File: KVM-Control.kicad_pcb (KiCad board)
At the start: 2 copper layers, 14 parts, among them J1 KVM 1, J2 KVM 2, J3 KVM 2, U1 ESP32-S3-DevKitC, U2 ULN2003A, U3 PC847, U5 L7805

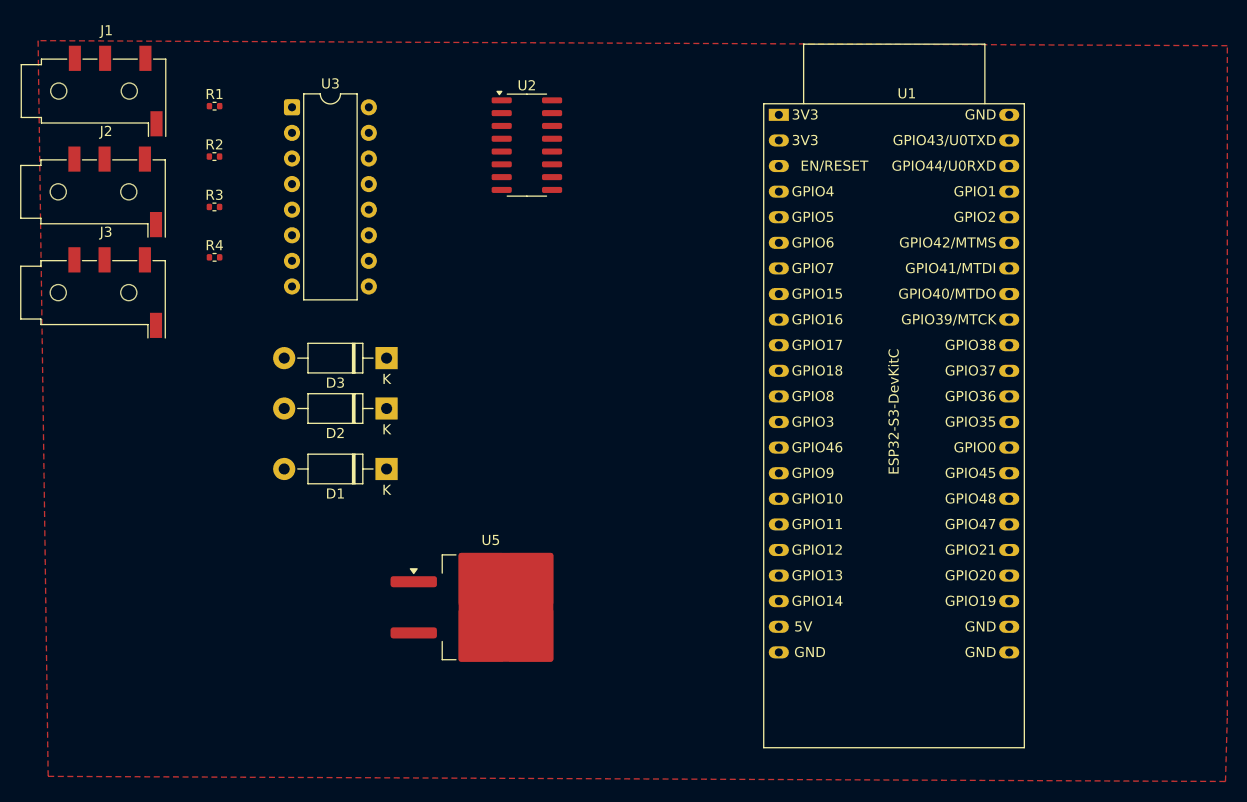
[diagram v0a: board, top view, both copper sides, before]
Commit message: Added status LEDs.
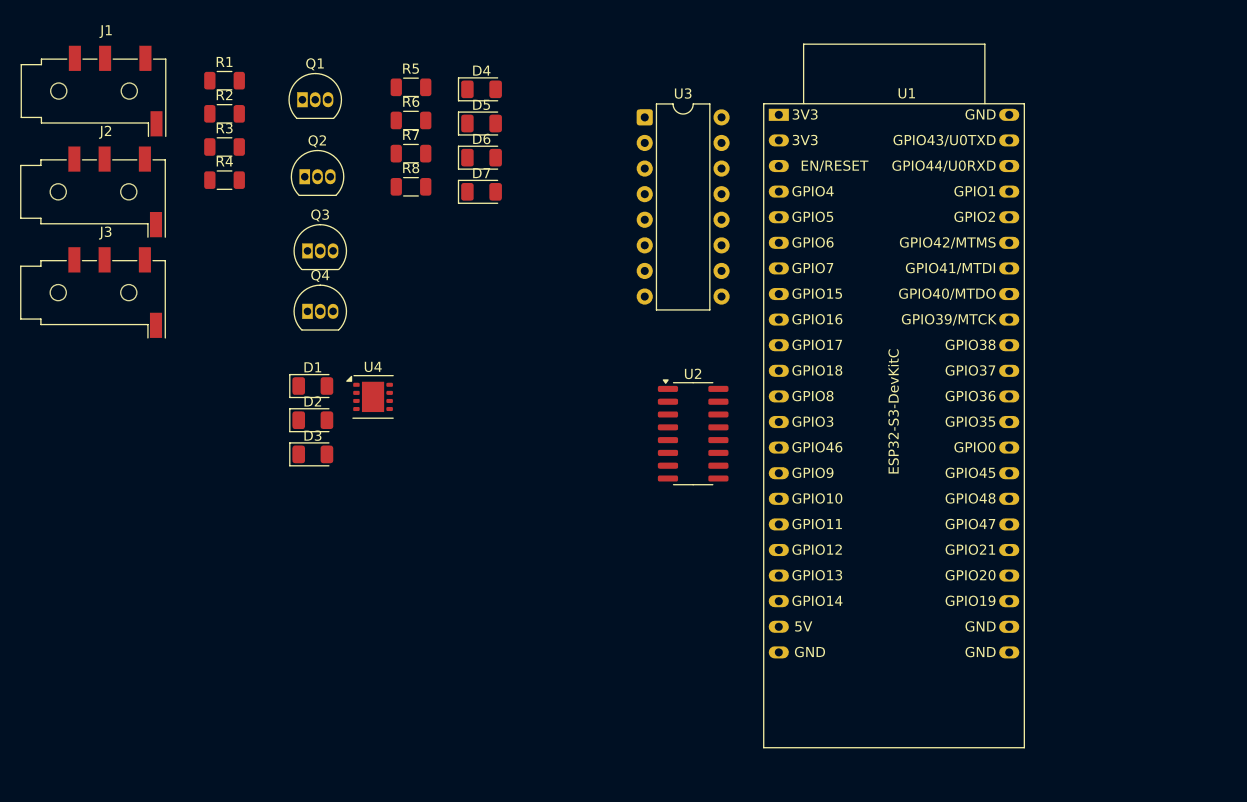
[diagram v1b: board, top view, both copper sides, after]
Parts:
- removed U5: L7805, Package_TO_SOT_SMD:TO-263-2
- added D4: LED, LED_SMD:LED_1206_3216Metric, F.Cu at (56.0, 16.8)
- added D5: LED, LED_SMD:LED_1206_3216Metric, F.Cu at (56.0, 20.2)
- added D6: LED, LED_SMD:LED_1206_3216Metric, F.Cu at (56.0, 23.6)
- added D7: LED, LED_SMD:LED_1206_3216Metric, F.Cu at (56.0, 27.0)
- added Q1: 2N3904, Package_TO_SOT_THT:TO-92_Inline, F.Cu at (38.2, 17.9)
- added Q2: 2N3904, Package_TO_SOT_THT:TO-92_Inline, F.Cu at (38.5, 25.5)
- added Q3: 2N3904, Package_TO_SOT_THT:TO-92_Inline, F.Cu at (38.7, 32.9)
- added Q4: 2N3904, Package_TO_SOT_THT:TO-92_Inline, F.Cu at (38.7, 38.9)
- added R5: 68Ω, Resistor_SMD:R_1206_3216Metric, F.Cu at (49.0, 16.6)
- added R6: 68Ω, Resistor_SMD:R_1206_3216Metric, F.Cu at (49.0, 19.9)
- added R7: 68Ω, Resistor_SMD:R_1206_3216Metric, F.Cu at (49.0, 23.2)
- added R8: 68Ω, Resistor_SMD:R_1206_3216Metric, F.Cu at (49.0, 26.5)
- added U4: LM1117LD-5.0, Package_SON:WSON-8-1EP_4x4mm_P0.8mm_EP2.2x3mm, F.Cu at (45.2, 47.4)
- D1, D2, D3: footprint Diode_THT:D_DO-41_SOD81_P10.16mm_Horizontal -> Diode_SMD:D_1206_3216Metric
- R1, R2, R3, R4: footprint Resistor_SMD:R_0402_1005Metric -> Resistor_SMD:R_1206_3216Metric
- moved U3 35.0 mm to (72.2, 19.6)
- moved U2 33.0 mm to (77.0, 51.0)
- moved D3 12.0 mm to (39.3, 53.0), turned to 0 degrees
- moved D1 11.0 mm to (39.3, 46.3), turned to 0 degrees
- moved R4 7.72 mm to (30.5, 25.8)
- moved D2 7.41 mm to (39.3, 49.7), turned to 0 degrees
- moved R3 6.03 mm to (30.5, 22.6)
- moved R2 4.36 mm to (30.5, 19.3)
- moved R1 2.72 mm to (30.5, 16.0)
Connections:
- net Net-(D1-A) renamed J1_POWER_5V
- net Net-(D2-A) renamed J2_POWER_5V
- net Net-(D3-A) renamed J3_POWER_5V
- R4 pad 1: unconnected-(R4-Pad1) -> J4_STATE
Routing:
- removed copper zone on F.Cu, net GND
